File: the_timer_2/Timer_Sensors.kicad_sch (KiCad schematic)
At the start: 6 parts, among them J6 BMI-S-209-F, U6 MS5607-02BA, U8 BMI088

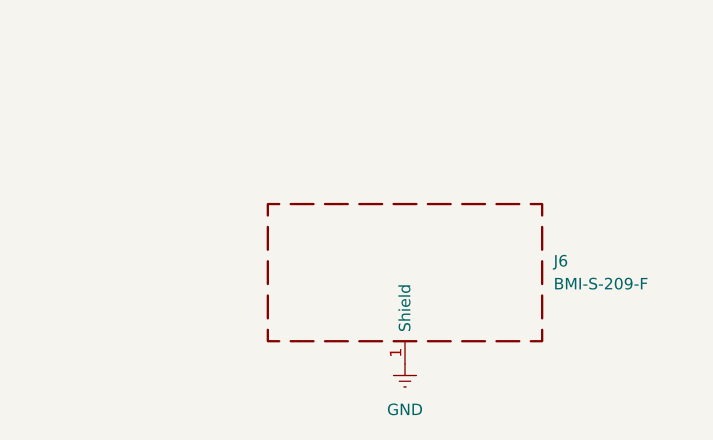
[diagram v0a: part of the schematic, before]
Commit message: Mostly de-exploded the schematic
Also like sorta fixed the PCB design but not really but sorta
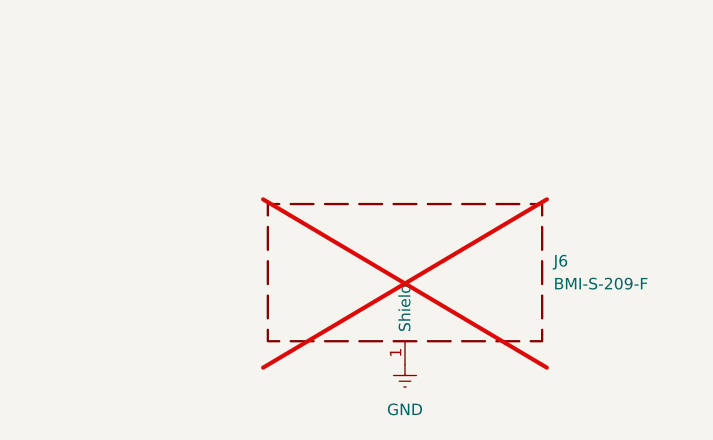
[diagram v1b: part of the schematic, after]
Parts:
- J6: now not fitted; now left out of the parts list
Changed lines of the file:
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@@
 		)
 		(instances
-			(project "the_timer_2"
+			(project "timer"
 				(path "/473e3a2e-6c5e-4995-af4a-e4bf1449cab0/a1a58bc4-7e65-411e-974f-12a034070c8b"
 					(reference "C11")
@@
 		)
 		(instances
-			(project "the_timer_2"
+			(project "timer"
 				(path "/473e3a2e-6c5e-4995-af4a-e4bf1449cab0/a1a58bc4-7e65-411e-974f-12a034070c8b"
 					(reference "#PWR065")
@@
 		)
 		(instances
-			(project "the_timer_2"
+			(project "timer"
 				(path "/473e3a2e-6c5e-4995-af4a-e4bf1449cab0/a1a58bc4-7e65-411e-974f-12a034070c8b"
 					(reference "#PWR062")
@@
 		)
 		(instances
-			(project "the_timer_2"
+			(project "timer"
 				(path "/473e3a2e-6c5e-4995-af4a-e4bf1449cab0/a1a58bc4-7e65-411e-974f-12a034070c8b"
 					(reference "C6")
@@
 		)
 		(instances
-			(project "the_timer_2"
+			(project "timer"
 				(path "/473e3a2e-6c5e-4995-af4a-e4bf1449cab0/a1a58bc4-7e65-411e-974f-12a034070c8b"
 					(reference "#PWR061")
@@
 		)
 		(instances
-			(project "the_timer_2"
+			(project "timer"
 				(path "/473e3a2e-6c5e-4995-af4a-e4bf1449cab0/a1a58bc4-7e65-411e-974f-12a034070c8b"
 					(reference "#PWR060")
@@
 		)
 		(instances
-			(project "the_timer_2"
+			(project "timer"
 				(path "/473e3a2e-6c5e-4995-af4a-e4bf1449cab0/a1a58bc4-7e65-411e-974f-12a034070c8b"
 					(reference "#PWR063")
@@
 		)
 		(instances
-			(project "the_timer_2"
+			(project "timer"
 				(path "/473e3a2e-6c5e-4995-af4a-e4bf1449cab0/a1a58bc4-7e65-411e-974f-12a034070c8b"
 					(reference "#PWR064")
@@
 		)
 		(instances
-			(project "the_timer_2"
+			(project "timer"
 				(path "/473e3a2e-6c5e-4995-af4a-e4bf1449cab0/a1a58bc4-7e65-411e-974f-12a034070c8b"
 					(reference "C12")
@@
 		)
 		(instances
-			(project "the_timer_2"
+			(project "timer"
 				(path "/473e3a2e-6c5e-4995-af4a-e4bf1449cab0/a1a58bc4-7e65-411e-974f-12a034070c8b"
 					(reference "#PWR052")
@@
 		)
 		(instances
-			(project "the_timer_2"
+			(project "timer"
 				(path "/473e3a2e-6c5e-4995-af4a-e4bf1449cab0/a1a58bc4-7e65-411e-974f-12a034070c8b"
 					(reference "#PWR049")
@@
 		)
 		(instances
-			(project "the_timer_2"
+			(project "timer"
 				(path "/473e3a2e-6c5e-4995-af4a-e4bf1449cab0/a1a58bc4-7e65-411e-974f-12a034070c8b"
 					(reference "U8")
@@
 		)
 		(instances
-			(project "the_timer_2"
+			(project "timer"
 				(path "/473e3a2e-6c5e-4995-af4a-e4bf1449cab0/a1a58bc4-7e65-411e-974f-12a034070c8b"
 					(reference "U6")
@@
 		(at 254 139.7 0)
 		(unit 1)
-		(exclude_from_sim no)
-		(in_bom yes)
-		(on_board yes)
-		(dnp no)
+		(exclude_from_sim yes)
+		(in_bom no)
+		(on_board no)
+		(dnp yes)
 		(fields_autoplaced yes)
 		(property "Reference" "J6"
@@
 		)
 		(instances
-			(project "the_timer_2"
+			(project "timer"
 				(path "/473e3a2e-6c5e-4995-af4a-e4bf1449cab0/a1a58bc4-7e65-411e-974f-12a034070c8b"
 					(reference "J6")
@@
 		)
 		(instances
-			(project "the_timer_2"
+			(project "timer"
 				(path "/473e3a2e-6c5e-4995-af4a-e4bf1449cab0/a1a58bc4-7e65-411e-974f-12a034070c8b"
 					(reference "#PWR03")
@@
 		)
 		(instances
-			(project "the_timer_2"
+			(project "timer"
 				(path "/473e3a2e-6c5e-4995-af4a-e4bf1449cab0/a1a58bc4-7e65-411e-974f-12a034070c8b"
 					(reference "#PWR01")
@@
 		)
 		(instances
-			(project "the_timer_2"
+			(project "timer"
 				(path "/473e3a2e-6c5e-4995-af4a-e4bf1449cab0/a1a58bc4-7e65-411e-974f-12a034070c8b"
 					(reference "#PWR053")
